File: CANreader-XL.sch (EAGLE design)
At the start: 77 parts, among them IC2 TJA1055T, IC3 BD9G101G, IC4 LM1117IMPX-3.3, IC5 STM32F107VBT, Q1 16MHz, SW1 SLEEP, SW2 TERM, U1 HC_05, U2 MCP2551, X1 MINI-USB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

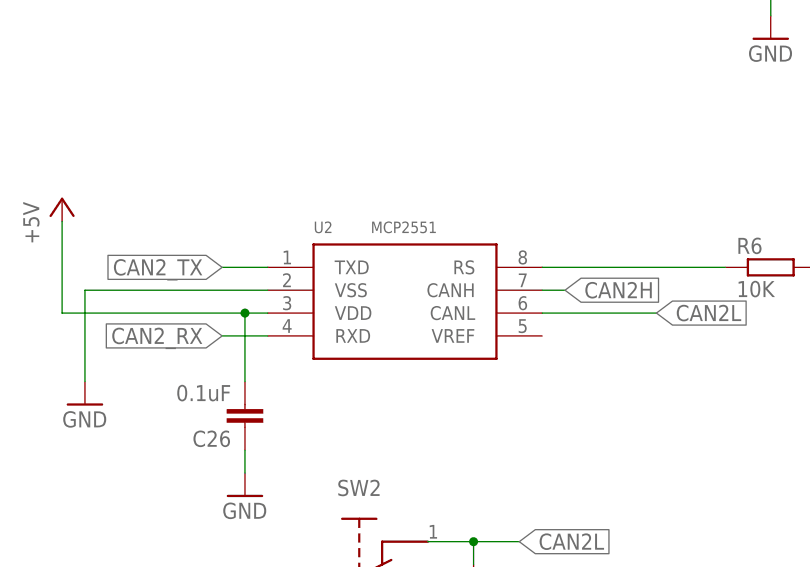
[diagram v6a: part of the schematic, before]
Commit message: Drop old lib
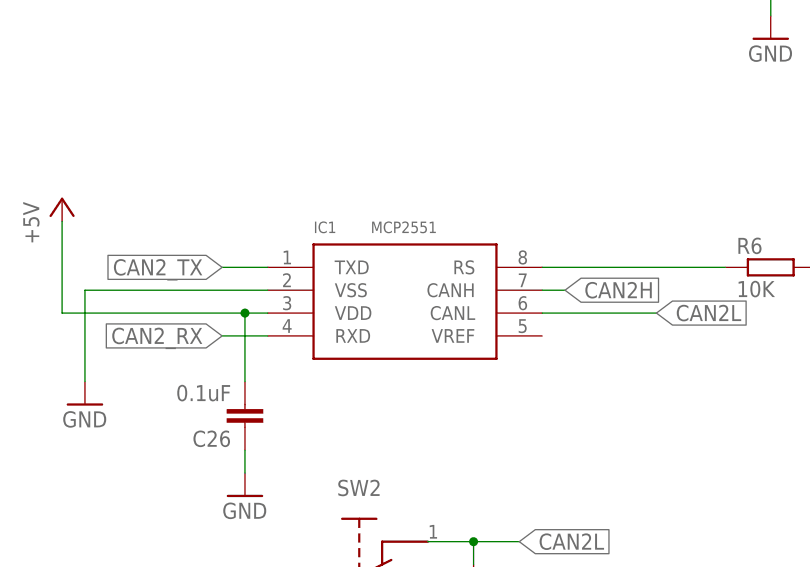
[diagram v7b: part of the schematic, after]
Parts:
- removed U2: MCP2551, CAN_Shiel_Lib:INTERFACE-MCP2551-I/SN(SOIC8)
- added IC1: MCP2551, STM32_CAN-USB:INTERFACE-MCP2551-I/SN(SOIC8)
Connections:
- net +5V: now also IC1.VDD; no longer U2.VDD
- net CAN2H: now also IC1.CANH; no longer U2.CANH
- net CAN2L: now also IC1.CANL; no longer U2.CANL
- net CAN2_RX: now also IC1.RXD; no longer U2.RXD
- net CAN2_TX: now also IC1.TXD; no longer U2.TXD
- net GND: now also IC1.VSS; no longer U2.VSS
- net N$5: now also IC1.RS; no longer U2.RS
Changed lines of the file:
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@@
 <layer number="99" name="SpiceOrder" color="5" fill="1" visible="yes" active="yes"/>
 <layer number="100" name="Muster" color="7" fill="1" visible="no" active="no"/>
-<layer number="101" name="Patch_Top" color="12" fill="4" visible="yes" active="yes"/>
 <layer number="102" name="Vscore" color="7" fill="1" visible="yes" active="yes"/>
 <layer number="103" name="tMap" color="7" fill="1" visible="no" active="no"/>
@@
 <layer number="112" name="tSilk" color="7" fill="1" visible="no" active="no"/>
 <layer number="113" name="IDFDebug" color="7" fill="1" visible="no" active="yes"/>
-<layer number="114" name="FRNTMAAT1" color="7" fill="1" visible="yes" active="yes"/>
-<layer number="115" name="FRNTMAAT2" color="7" fill="1" visible="yes" active="yes"/>
-<layer number="116" name="Patch_BOT" color="9" fill="4" visible="yes" active="yes"/>
-<layer number="117" name="BACKMAAT1" color="7" fill="1" visible="yes" active="yes"/>
 <layer number="118" name="Rect_Pads" color="7" fill="1" visible="no" active="no"/>
-<layer number="119" name="KAP_TEKEN" color="7" fill="1" visible="yes" active="yes"/>
-<layer number="120" name="KAP_MAAT1" color="7" fill="1" visible="yes" active="yes"/>
-<layer number="121" name="_tsilk" color="7" fill="1" visible="yes" active="yes"/>
-<layer number="122" name="_bsilk" color="7" fill="1" visible="yes" active="yes"/>
 <layer number="123" name="tTestmark" color="7" fill="1" visible="no" active="no"/>
 <layer number="124" name="bTestmark" color="7" fill="1" visible="no" active="no"/>
@@
 <layer number="127" name="_tValues" color="7" fill="1" visible="no" active="no"/>
 <layer number="128" name="_bValues" color="7" fill="1" visible="no" active="no"/>
-<layer number="129" name="top_silk" color="7" fill="1" visible="yes" active="yes"/>
-<layer number="130" name="SMDSTROOK" color="7" fill="1" visible="yes" active="yes"/>
 <layer number="131" name="tAdjust" color="7" fill="1" visible="no" active="no"/>
 <layer number="132" name="bAdjust" color="7" fill="1" visible="no" active="no"/>
-<layer number="133" name="bottom_silk" color="7" fill="1" visible="yes" active="yes"/>
 <layer number="144" name="DrillLegend" color="7" fill="1" visible="no" active="no"/>
 <layer number="150" name="Notes" color="7" fill="1" visible="no" active="yes"/>
-<layer number="151" name="HeatSink" color="7" fill="1" visible="yes" active="yes"/>
 <layer number="152" name="_bDocu" color="7" fill="1" visible="no" active="no"/>
 <layer number="153" name="FabDoc1" color="6" fill="1" visible="no" active="no"/>
@@
 <layer number="223" name="223bmp" color="24" fill="1" visible="no" active="no"/>
 <layer number="224" name="224bmp" color="25" fill="1" visible="no" active="no"/>
-<layer number="225" name="225bmp" color="7" fill="1" visible="no" active="yes"/>
-<layer number="226" name="226bmp" color="7" fill="1" visible="no" active="yes"/>
-<layer number="227" name="227bmp" color="7" fill="1" visible="no" active="yes"/>
-<layer number="228" name="228bmp" color="7" fill="1" visible="no" active="yes"/>
-<layer number="229" name="229bmp" color="7" fill="1" visible="yes" active="yes"/>
-<layer number="230" name="230bmp" color="7" fill="1" visible="no" active="yes"/>
-<layer number="231" name="Eagle3D_PG1" color="7" fill="1" visible="yes" active="yes"/>
-<layer number="232" name="Eagle3D_PG2" color="7" fill="1" visible="yes" active="yes"/>
-<layer number="233" name="Eagle3D_PG3" color="7" fill="1" visible="yes" active="yes"/>
 <layer number="248" name="Housing" color="7" fill="1" visible="no" active="no"/>
 <layer number="249" name="Edge" color="7" fill="1" visible="no" active="no"/>
@@
 <part name="C26" library="rcl" deviceset="C-EU" device="C0805" value="0.1uF"/>
 <part name="GND26" library="supply1" deviceset="GND" device=""/>
-<part name="U2" library="CAN_Shiel_Lib" deviceset="INTERFACE-MCP2551-I/SN(SOIC8)" device="" value="MCP2551"/>
 <part name="R6" library="rcl" deviceset="R-EU_" device="R0805" value="10K"/>
 <part name="GND27" library="supply1" deviceset="GND" device=""/>
@@
 <part name="X4" library="STM32_CAN-USB" deviceset="PINHD-1X4" device="/90" value="UART"/>
 <part name="X2" library="STM32_CAN-USB" deviceset="PINHD-1X4" device="" value="SWD"/>
+<part name="IC1" library="STM32_CAN-USB" deviceset="INTERFACE-MCP2551-I/SN(SOIC8)" device="" value="MCP2551"/>
 </parts>
 <sheets>
@@
 <instance part="C26" gate="G$1" x="-68.58" y="-86.36" rot="R180"/>
 <instance part="GND26" gate="1" x="-68.58" y="-93.98"/>
-<instance part="U2" gate="G$1" x="-50.8" y="-73.66"/>
 <instance part="R6" gate="G$1" x="-10.16" y="-68.58"/>
 <instance part="GND27" gate="1" x="-2.54" y="-76.2"/>
@@
 <instance part="X4" gate="A" x="-22.86" y="-5.08"/>
 <instance part="X2" gate="A" x="-66.04" y="68.58"/>
+<instance part="IC1" gate="G$1" x="-50.8" y="-72.39"/>
 </instances>
 <busses>
@@
 <pinref part="GND28" gate="1" pin="GND"/>
 <wire x1="-86.36" y1="-81.28" x2="-86.36" y2="-71.12" width="0.1524" layer="91"/>
-<pinref part="U2" gate="G$1" pin="VSS"/>
 <wire x1="-86.36" y1="-71.12" x2="-66.04" y2="-71.12" width="0.1524" layer="91"/>
+<pinref part="IC1" gate="G$1" pin="VSS"/>
 </segment>
 <segment>
@@
 <pinref part="P+8" gate="1" pin="+5V"/>
 <wire x1="-88.9" y1="-63.5" x2="-88.9" y2="-73.66" width="0.1524" layer="91"/>
-<pinref part="U2" gate="G$1" pin="VDD"/>
 <wire x1="-66.04" y1="-73.66" x2="-68.58" y2="-73.66" width="0.1524" layer="91"/>
 <pinref part="C26" gate="G$1" pin="2"/>
@@
 <wire x1="-68.58" y1="-81.28" x2="-68.58" y2="-73.66" width="0.1524" layer="91"/>
 <junction x="-68.58" y="-73.66"/>
+<pinref part="IC1" gate="G$1" pin="VDD"/>
 </segment>
 </net>
@@
 <net name="N$5" class="0">
 <segment>
-<pinref part="U2" gate="G$1" pin="RS"/>
 <pinref part="R6" gate="G$1" pin="1"/>
 <wire x1="-35.56" y1="-68.58" x2="-15.24" y2="-68.58" width="0.1524" layer="91"/>
+<pinref part="IC1" gate="G$1" pin="RS"/>
 </segment>
 </net>
 <net name="CAN2_TX" class="0">
 <segment>
-<pinref part="U2" gate="G$1" pin="TXD"/>
 <wire x1="-66.04" y1="-68.58" x2="-71.12" y2="-68.58" width="0.1524" layer="91"/>
 <label x="-71.12" y="-68.58" size="1.778" layer="95" rot="R180" xref="yes"/>
+<pinref part="IC1" gate="G$1" pin="TXD"/>
 </segment>
 <segment>
@@
 <net name="CAN2_RX" class="0">
 <segment>
-<pinref part="U2" gate="G$1" pin="RXD"/>
 <wire x1="-66.04" y1="-76.2" x2="-71.12" y2="-76.2" width="0.1524" layer="91"/>
 <label x="-71.12" y="-76.2" size="1.778" layer="95" rot="R180" xref="yes"/>
+<pinref part="IC1" gate="G$1" pin="RXD"/>
 </segment>
 <segment>
@@
 <net name="CAN2L" class="0">
 <segment>
-<pinref part="U2" gate="G$1" pin="CANL"/>
 <wire x1="-35.56" y1="-73.66" x2="-22.86" y2="-73.66" width="0.1524" layer="91"/>
 <label x="-22.86" y="-73.66" size="1.778" layer="95" xref="yes"/>
+<pinref part="IC1" gate="G$1" pin="CANL"/>
 </segment>
 <segment>
@@
 <net name="CAN2H" class="0">
 <segment>
-<pinref part="U2" gate="G$1" pin="CANH"/>
 <wire x1="-35.56" y1="-71.12" x2="-33.02" y2="-71.12" width="0.1524" layer="91"/>
 <label x="-33.02" y="-71.12" size="1.778" layer="95" xref="yes"/>
-</segment>
-<segment>
+<pinref part="IC1" gate="G$1" pin="CANH"/>
+</segment>
+<segment>
